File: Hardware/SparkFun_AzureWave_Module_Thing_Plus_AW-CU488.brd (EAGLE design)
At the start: 22.9 x 77.5 mm, 123 parts, among them J1 THING_PLUS, J3 QWIIC_RA, J5 USB-C, Q1 3.1A/30V/105mΩ, Q2 MBT3904DW1T1, U2 CP210X, U3 AP2112K-3.3V, U4 MCP73831

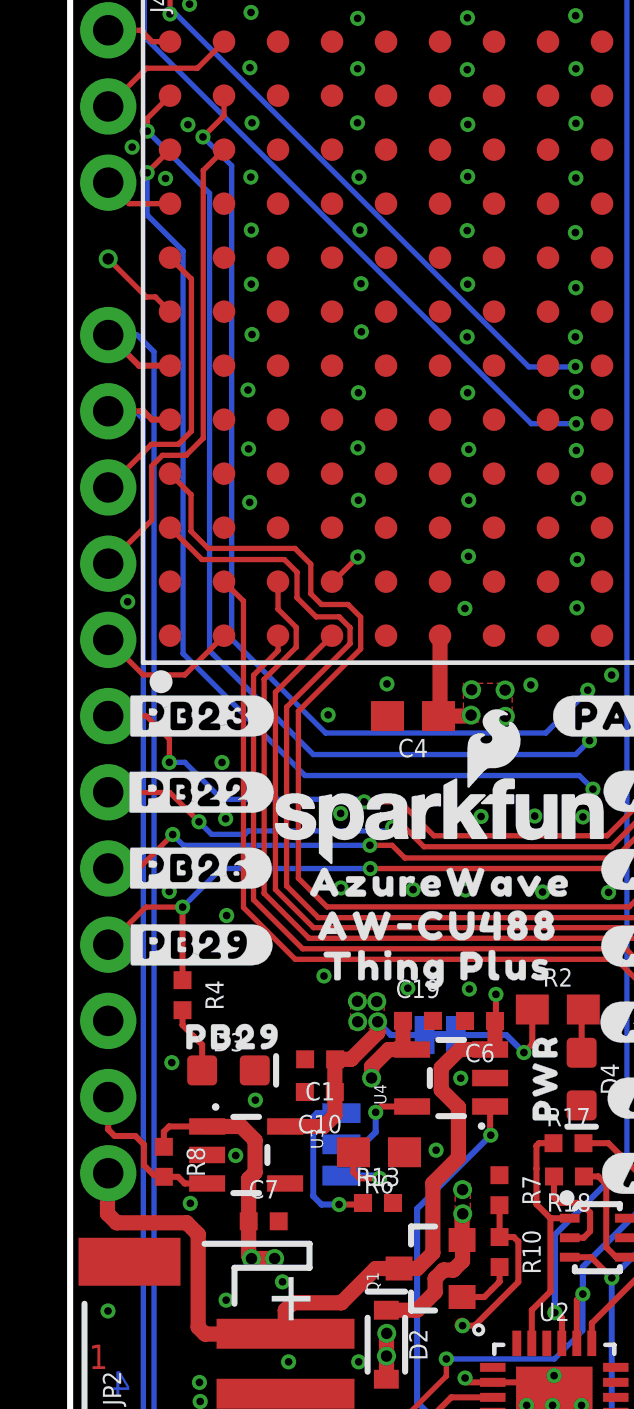
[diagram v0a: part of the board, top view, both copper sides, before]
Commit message: final check finds
-Scooted VIN trace for GND flow near Vreg
-nudged trace off of PA27 to avoid acid trap
-updated pin names to include SWD functions in symbol
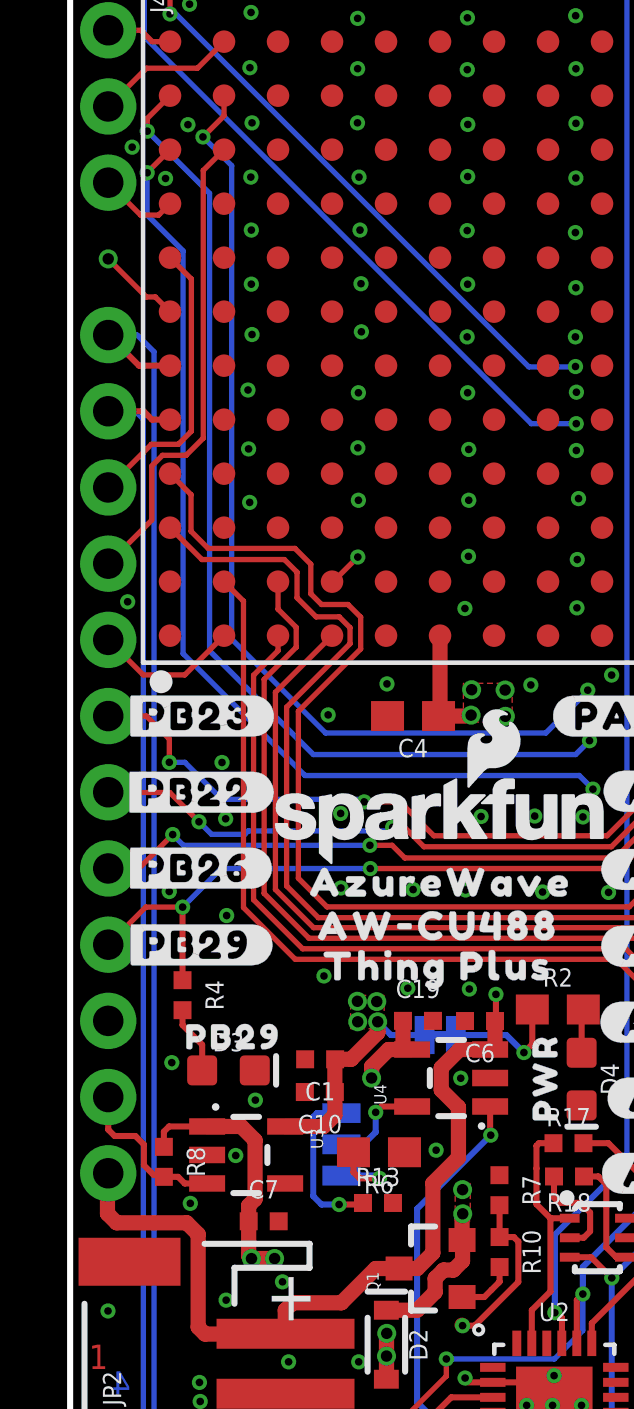
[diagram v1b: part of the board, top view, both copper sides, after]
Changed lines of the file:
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@@
 <drawing>
 <settings>
-<setting alwaysvectorfont="no"/>
+<setting alwaysvectorfont="yes"/>
 <setting keepoldvectorfont="yes"/>
 <setting verticaltext="up"/>
 </settings>
-<grid distance="0.05" unitdist="inch" unit="inch" style="lines" multiple="1" display="yes" altdistance="0.0001" altunitdist="inch" altunit="inch"/>
+<grid distance="0.05" unitdist="inch" unit="mm" style="lines" multiple="1" display="yes" altdistance="0.005" altunitdist="inch" altunit="inch"/>
 <layers>
 <layer number="1" name="Top" color="4" fill="1" visible="yes" active="yes"/>
 <layer number="2" name="Route2" color="1" fill="3" visible="no" active="yes"/>
 <layer number="15" name="Route15" color="4" fill="6" visible="no" active="yes"/>
-<layer number="16" name="Bottom" color="1" fill="1" visible="yes" active="yes"/>
+<layer number="16" name="Bottom" color="1" fill="1" visible="no" active="yes"/>
 <layer number="17" name="Pads" color="2" fill="1" visible="yes" active="yes"/>
-<layer number="18" name="Vias" color="2" fill="1" visible="yes" active="yes"/>
-<layer number="19" name="Unrouted" color="6" fill="1" visible="yes" active="yes"/>
+<layer number="18" name="Vias" color="2" fill="1" visible="no" active="yes"/>
+<layer number="19" name="Unrouted" color="6" fill="1" visible="no" active="yes"/>
 <layer number="20" name="Dimension" color="24" fill="1" visible="yes" active="yes"/>
 <layer number="21" name="tPlace" color="16" fill="1" visible="yes" active="yes"/>
-<layer number="22" name="bPlace" color="14" fill="1" visible="yes" active="yes"/>
-<layer number="23" name="tOrigins" color="15" fill="1" visible="yes" active="yes"/>
-<layer number="24" name="bOrigins" color="15" fill="1" visible="yes" active="yes"/>
+<layer number="22" name="bPlace" color="14" fill="1" visible="no" active="yes"/>
+<layer number="23" name="tOrigins" color="15" fill="1" visible="no" active="yes"/>
+<layer number="24" name="bOrigins" color="15" fill="1" visible="no" active="yes"/>
 <layer number="25" name="tNames" color="7" fill="1" visible="no" active="yes"/>
 <layer number="26" name="bNames" color="7" fill="1" visible="no" active="yes"/>
@@
 <layer number="43" name="vRestrict" color="2" fill="10" visible="no" active="yes"/>
 <layer number="44" name="Drills" color="7" fill="1" visible="no" active="yes"/>
-<layer number="45" name="Holes" color="7" fill="1" visible="yes" active="yes"/>
+<layer number="45" name="Holes" color="7" fill="1" visible="no" active="yes"/>
 <layer number="46" name="Milling" color="3" fill="1" visible="no" active="yes"/>
-<layer number="47" name="Measures" color="7" fill="1" visible="no" active="yes"/>
+<layer number="47" name="Measures" color="7" fill="1" visible="yes" active="yes"/>
 <layer number="48" name="Document" color="7" fill="1" visible="no" active="yes"/>
-<layer number="49" name="Reference" color="7" fill="1" visible="yes" active="yes"/>
+<layer number="49" name="Reference" color="7" fill="1" visible="no" active="yes"/>
 <layer number="51" name="tDocu" color="6" fill="1" visible="yes" active="yes"/>
 <layer number="52" name="bDocu" color="7" fill="1" visible="no" active="yes"/>
@@
 <wire x1="6.0452" y1="21.2852" x2="6.055359375" y2="21.295359375" width="0.508" layer="15"/>
 <via x="6.0452" y="21.2852" extent="1-16" drill="0.381"/>
-<wire x1="6.1642" y1="25.2302" x2="6.1642" y2="24.1554" width="0.508" layer="1"/>
+<wire x1="6.1642" y1="25.2302" x2="6.1642" y2="23.2664" width="0.508" layer="1"/>
 <wire x1="5.7048" y1="25.6896" x2="4.5673" y2="25.6896" width="0.508" layer="1"/>
 <wire x1="6.1642" y1="25.2302" x2="5.7048" y2="25.6896" width="0.508" layer="1"/>
@@
 <wire x1="3.296959375" y1="25.6896" x2="4.5673" y2="25.6896" width="0.2032" layer="1"/>
 <wire x1="3.1242" y1="25.516840625" x2="3.296959375" y2="25.6896" width="0.2032" layer="1"/>
-<wire x1="5.9516" y1="23.9428" x2="5.9516" y2="22.5298" width="0.508" layer="1"/>
-<wire x1="6.1642" y1="24.1554" x2="5.9516" y2="23.9428" width="0.508" layer="1"/>
+<wire x1="5.9516" y1="23.0538" x2="5.9516" y2="22.5298" width="0.508" layer="1"/>
+<wire x1="6.1642" y1="23.2664" x2="5.9516" y2="23.0538" width="0.508" layer="1"/>
 <wire x1="5.9516" y1="22.5298" x2="5.9516" y2="21.3788" width="0.508" layer="1"/>
 <wire x1="5.9516" y1="21.3788" x2="6.0452" y2="21.2852" width="0.508" layer="1"/>
@@
 <contactref element="U$13" pad="A9"/>
 <contactref element="J4" pad="3"/>
-<wire x1="3.33" y1="56.45" x2="1.97" y2="56.45" width="0.1778" layer="1"/>
-<wire x1="1.97" y1="56.45" x2="1.27" y2="57.15" width="0.1778" layer="1"/>
+<wire x1="3.33" y1="56.45" x2="2.949" y2="56.069" width="0.1778" layer="1"/>
+<wire x1="2.949" y1="56.069" x2="2.351" y2="56.069" width="0.1778" layer="1"/>
+<wire x1="2.351" y1="56.069" x2="1.27" y2="57.15" width="0.1778" layer="1"/>
 </signal>
 <signal name="PA30">

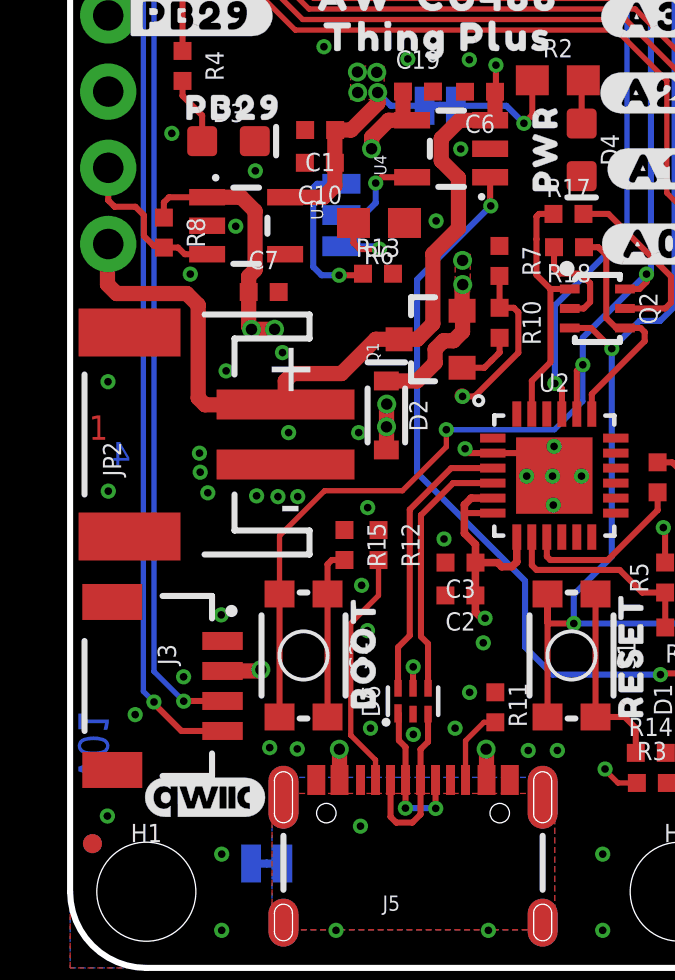
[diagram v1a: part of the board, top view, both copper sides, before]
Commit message: Re-routed traces off of charge current select jumper
-The traces were unnecessarily tight off the jumpers and easy to cut on accident. Now they have more clearance.
-Also bumped version to v10 in brd and sch
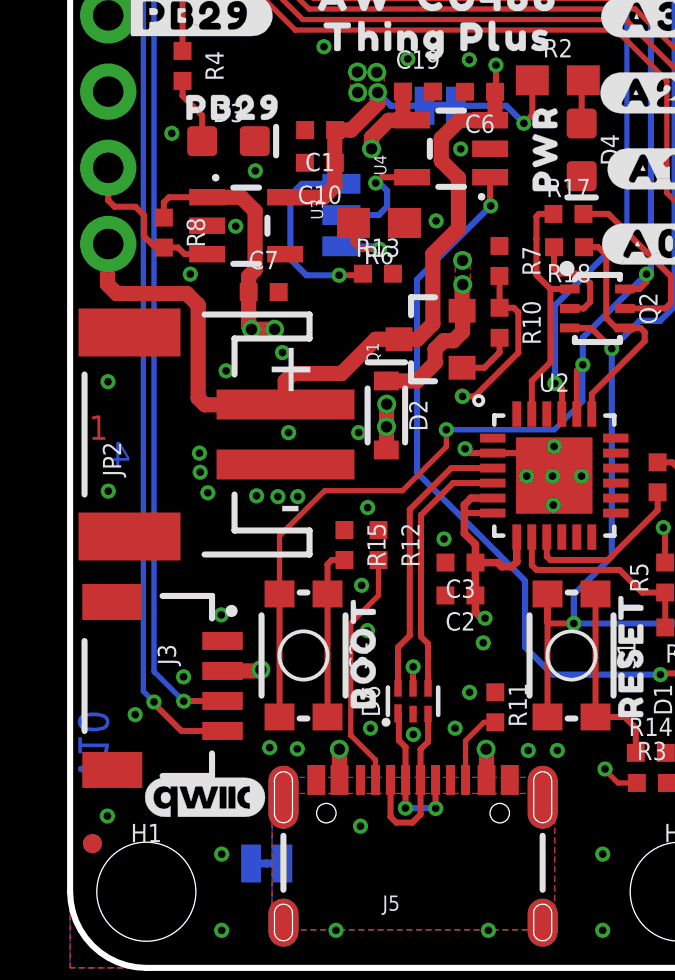
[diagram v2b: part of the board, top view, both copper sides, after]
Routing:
- net N$11: track 5.43 -> 6.66 mm
- net N$9: track 3.27 -> 3.95 mm
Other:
- board text added: "v10"
- board text removed: "v01"
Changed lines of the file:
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@@
 <drawing>
 <settings>
-<setting alwaysvectorfont="yes"/>
+<setting alwaysvectorfont="no"/>
 <setting keepoldvectorfont="yes"/>
 <setting verticaltext="up"/>
 </settings>
-<grid distance="0.05" unitdist="inch" unit="mm" style="lines" multiple="1" display="yes" altdistance="0.005" altunitdist="inch" altunit="inch"/>
+<grid distance="0.05" unitdist="inch" unit="inch" style="lines" multiple="1" display="yes" altdistance="0.005" altunitdist="inch" altunit="inch"/>
 <layers>
 <layer number="1" name="Top" color="4" fill="1" visible="yes" active="yes"/>
 <layer number="2" name="Route2" color="1" fill="3" visible="no" active="yes"/>
 <layer number="15" name="Route15" color="4" fill="6" visible="no" active="yes"/>
-<layer number="16" name="Bottom" color="1" fill="1" visible="no" active="yes"/>
+<layer number="16" name="Bottom" color="1" fill="1" visible="yes" active="yes"/>
 <layer number="17" name="Pads" color="2" fill="1" visible="yes" active="yes"/>
-<layer number="18" name="Vias" color="2" fill="1" visible="no" active="yes"/>
-<layer number="19" name="Unrouted" color="6" fill="1" visible="no" active="yes"/>
+<layer number="18" name="Vias" color="2" fill="1" visible="yes" active="yes"/>
+<layer number="19" name="Unrouted" color="6" fill="1" visible="yes" active="yes"/>
 <layer number="20" name="Dimension" color="24" fill="1" visible="yes" active="yes"/>
 <layer number="21" name="tPlace" color="16" fill="1" visible="yes" active="yes"/>
-<layer number="22" name="bPlace" color="14" fill="1" visible="no" active="yes"/>
-<layer number="23" name="tOrigins" color="15" fill="1" visible="no" active="yes"/>
-<layer number="24" name="bOrigins" color="15" fill="1" visible="no" active="yes"/>
+<layer number="22" name="bPlace" color="14" fill="1" visible="yes" active="yes"/>
+<layer number="23" name="tOrigins" color="15" fill="1" visible="yes" active="yes"/>
+<layer number="24" name="bOrigins" color="15" fill="1" visible="yes" active="yes"/>
 <layer number="25" name="tNames" color="7" fill="1" visible="no" active="yes"/>
 <layer number="26" name="bNames" color="7" fill="1" visible="no" active="yes"/>
@@
 <layer number="43" name="vRestrict" color="2" fill="10" visible="no" active="yes"/>
 <layer number="44" name="Drills" color="7" fill="1" visible="no" active="yes"/>
-<layer number="45" name="Holes" color="7" fill="1" visible="no" active="yes"/>
+<layer number="45" name="Holes" color="7" fill="1" visible="yes" active="yes"/>
 <layer number="46" name="Milling" color="3" fill="1" visible="no" active="yes"/>
-<layer number="47" name="Measures" color="7" fill="1" visible="yes" active="yes"/>
+<layer number="47" name="Measures" color="7" fill="1" visible="no" active="yes"/>
 <layer number="48" name="Document" color="7" fill="1" visible="no" active="yes"/>
-<layer number="49" name="Reference" color="7" fill="1" visible="no" active="yes"/>
+<layer number="49" name="Reference" color="7" fill="1" visible="yes" active="yes"/>
 <layer number="51" name="tDocu" color="6" fill="1" visible="yes" active="yes"/>
 <layer number="52" name="bDocu" color="7" fill="1" visible="no" active="yes"/>
@@
 <wire x1="2.54" y1="0" x2="20.32" y2="0" width="0.2032" layer="20"/>
 <wire x1="20.32" y1="0" x2="22.86" y2="2.54" width="0.2032" layer="20" curve="90"/>
-<text x="0.782321875" y="8.5979" size="1.016" layer="16" font="vector" ratio="20" rot="MR270" align="center-left">v01</text>
+<text x="0.782321875" y="8.5979" size="1.016" layer="16" font="vector" ratio="20" rot="MR270" align="center-left">v10</text>
 <text x="0.6223" y="17.604740625" size="0.8128" layer="1" font="vector" ratio="25">1</text>
 <text x="1.3843" y="17.604740625" size="0.8128" layer="2" font="vector" ratio="25">2</text>
@@
 <wire x1="10.3784" y1="26.355" x2="10.1854" y2="26.162" width="0.2032" layer="1"/>
 <via x="10.1854" y="26.162" extent="1-16" drill="0.254"/>
-<wire x1="10.1854" y1="26.162" x2="10.1854" y2="25.5016" width="0.2032" layer="16"/>
-<wire x1="10.1854" y1="25.5016" x2="9.779" y2="25.0952" width="0.2032" layer="16"/>
-<wire x1="9.779" y1="25.0952" x2="9.0424" y2="25.0952" width="0.2032" layer="16"/>
+<wire x1="10.5664" y1="25.908" x2="10.3124" y2="26.162" width="0.2032" layer="16"/>
+<wire x1="10.1854" y1="26.162" x2="10.3124" y2="26.162" width="0.2032" layer="16"/>
+<wire x1="10.5664" y1="25.908" x2="10.5664" y2="25.3746" width="0.2032" layer="16"/>
+<wire x1="10.5664" y1="25.3746" x2="10.287" y2="25.0952" width="0.2032" layer="16"/>
+<wire x1="10.287" y1="25.0952" x2="9.0424" y2="25.0952" width="0.2032" layer="16"/>
 </signal>
 <signal name="N$11">
@@
 <wire x1="9.7616" y1="23.1394" x2="9.7108" y2="23.0886" width="0.2032" layer="1"/>
 <wire x1="9.7108" y1="23.0886" x2="8.9662" y2="23.0886" width="0.2032" layer="1"/>
-<wire x1="9.0424" y1="26.1366" x2="8.2296" y2="26.1366" width="0.2032" layer="16"/>
-<wire x1="8.2296" y1="26.1366" x2="8.1026" y2="26.0096" width="0.2032" layer="16"/>
-<wire x1="8.1026" y1="26.0096" x2="8.1026" y2="23.368" width="0.2032" layer="16"/>
-<wire x1="8.382" y1="23.0886" x2="8.9662" y2="23.0886" width="0.2032" layer="16"/>
-<wire x1="8.1026" y1="23.368" x2="8.382" y2="23.0886" width="0.2032" layer="16"/>
+<wire x1="9.0424" y1="26.1366" x2="7.7216" y2="26.1366" width="0.2032" layer="16"/>
+<wire x1="7.7216" y1="26.1366" x2="7.3406" y2="25.7556" width="0.2032" layer="16"/>
+<wire x1="7.3406" y1="25.7556" x2="7.3406" y2="23.622" width="0.2032" layer="16"/>
+<wire x1="7.874" y1="23.0886" x2="8.9662" y2="23.0886" width="0.2032" layer="16"/>
+<wire x1="7.3406" y1="23.622" x2="7.874" y2="23.0886" width="0.2032" layer="16"/>
 </signal>
 <signal name="N$13">
